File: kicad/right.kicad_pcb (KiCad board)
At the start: 4 copper layers, 127.3 x 89.6 mm, 159 parts, among them M2 MountingHole_2.2mm_M2, Q1 PMF170XP,115, Q2 FS8205A_C2830320, SW1 TS-1088-AR02016, U1 TLV7031QDCKRQ1, U2 E73-2G4M08S1C, U3 SN74LVC1G74DQER, U4 S2B-PH-K-S(LF)(SN), U5 BL8573CS8TR, U6 DW01A_C42380662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

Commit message: started left
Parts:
- moved REF** 0.21 mm to (58.0, 38.2)
- moved USBC1 0.05 mm to (51.5, 30.7)

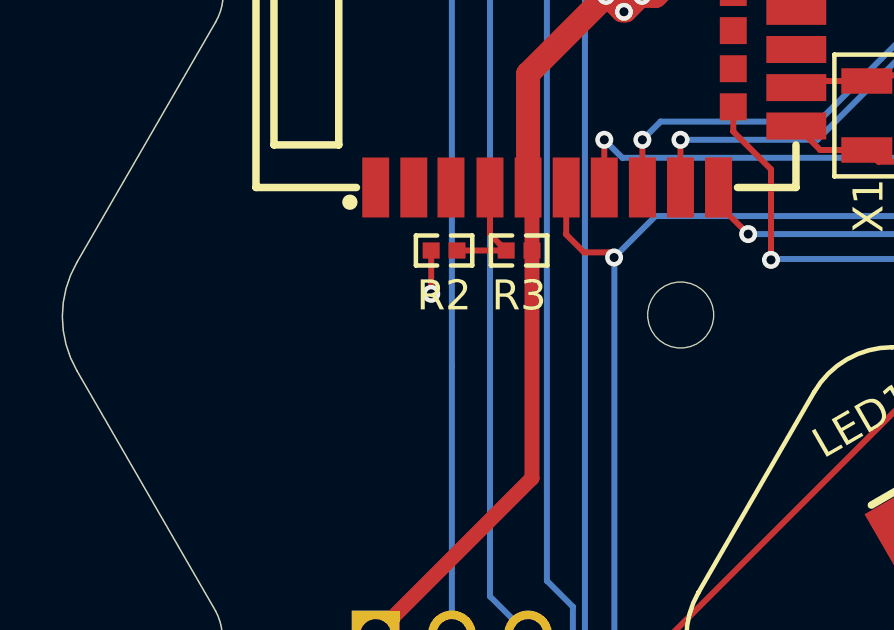
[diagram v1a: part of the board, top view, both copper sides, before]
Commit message: moved  one mounting hole
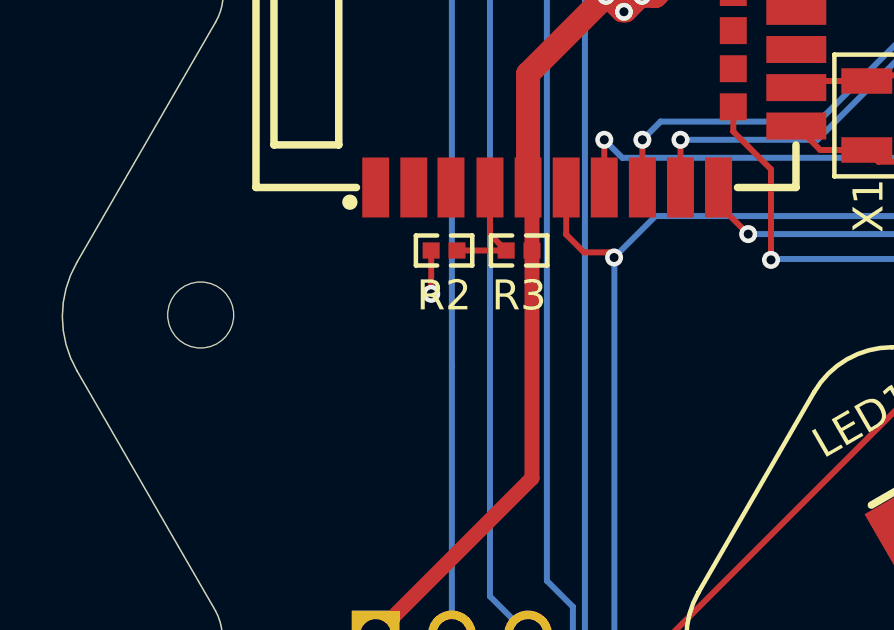
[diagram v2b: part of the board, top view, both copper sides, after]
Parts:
- moved REF** 16.0 mm to (24.7, 91.9)
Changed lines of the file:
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@@
 	(footprint "MountingHole:MountingHole_2.2mm_M2"
 		(layer "F.Cu")
-		(at 40.7 91.9174)
+		(at 24.7 91.9174)
 		(descr "Mounting Hole 2.2mm, M2, no annular, generated by kicad-footprint-generator mountinghole.py")
 		(tags "mountinghole M2")

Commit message: ...
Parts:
- added R17: RC0402FR-071ML, easyeda2kicad:R0402, B.Cu at (43.7, 58.9)
- added R18: WR04W2494FTL, easyeda2kicad:R0402, B.Cu at (41.5, 58.9)
- moved H1 5.00 mm to (33.1, 97.6)
- moved L1 1.08 mm to (46.5, 74.4)
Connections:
- U2 pad 1: /COL7 -> /SWBCLK
- U2 pad 15: unconnected-(U2-AI3-Pad15) -> /LED_EN
- U2 pad 16: unconnected-(U2-P0.08-Pad16) -> /LED_SDA
- U2 pad 17: /COL6 -> /LED_SCL
- U2 pad 2: unconnected-(U2-P1.10-Pad2) -> /SWDIO
- U2 pad 37: /SWDIO -> unconnected-(U2-SWD-Pad37)
- U2 pad 39: /SWBCLK -> unconnected-(U2-SWC-Pad39)
- U2 pad 40: unconnected-(U2-P1.04-Pad40) -> /PWR_BTN_PRESS
- U2 pad 7: /LED_EN -> unconnected-(U2-AI0-Pad7)
- U2 pad 8: /LED_SDA -> unconnected-(U2-AI5-Pad8)
- U2 pad 9: /LED_SCL -> /ROW4
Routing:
- net /ROW4: track 76.2 -> 104.4 mm, vias 0 -> 1
- net /PWR_BTN_PRESS: track 0.00 -> 28.0 mm, vias 0 -> 1
- net /SWBCLK: track 31.3 -> 11.0 mm, vias 1 -> 0
- net /SWDIO: track 31.9 -> 12.3 mm, vias 1 -> 0
- net GND: track 125.1 -> 110.7 mm, vias 47 -> 49
- net /LED_EN: track 20.7 -> 9.42 mm, vias 2 -> 0
- net /LED_SCL: track 17.0 -> 9.77 mm, vias 2 -> 0
- net /LED_SDA: track 19.9 -> 15.3 mm
- net /PWR_BTN: track 32.6 -> 35.0 mm
- net /COL5: track 118.9 -> 119.8 mm
- net Net-(U2-DCH): track 1.93 -> 2.73 mm
- net /VDD_nRF: track 54.0 -> 53.3 mm
- net /PWR: track 92.5 -> 93.0 mm

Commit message: left wiring done... right changed to shmitt inctead of comparator... need to do same on left... fixing of right in progress
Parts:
- removed the R4 at (56.3, 56.9)
- removed the R5 at (49.3, 58.8)
- removed component_case_outline (x5), component_safe_space (x3): , hexcaps:PG1350_hotswap
- R6: value RC0402FR-071ML -> 0402WGF1604TCE
- U1: value TLV7031QDCKRQ1 -> SN74LVC1G17DBVR; footprint easyeda2kicad:SC-70-5_L2.0-W1.3-P0.65-LS2.1-BR -> easyeda2kicad:SOT-23-5_L3.0-W1.7-P0.95-LS2.8-BR
- moved R6 6.85 mm to (56.2, 56.9), turned to -90 degrees
- moved U1 1.12 mm to (51.6, 58.9), turned to 180 degrees
- renumbered R17 to R1, R18 to R2, R1 to R3, R2 to R4, R3 to R5
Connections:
- C2 pad 1: Net-(U1-IN+) -> Net-(U1-A)
- D1 pad 2: Net-(U1-IN+) -> Net-(U1-A)
- R6 pad 2: Net-(U1-IN-) -> Net-(U1-A)
- U1 pad 1: Net-(U1-OUT) -> unconnected-(U1-N.C-Pad1)
- U1 pad 2: GND -> Net-(U1-A)
- U1 pad 3: Net-(U1-IN+) -> GND
- U1 pad 4: Net-(U1-IN-) -> Net-(U1-Y)
- U3 pad 1: Net-(U1-OUT) -> Net-(U1-Y)
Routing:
- net Net-(U1-A): track 0.00 -> 7.23 mm
- net Net-(U1-IN+): track 4.11 -> 0.00 mm
- net Net-(U1-IN-): track 2.86 -> 0.00 mm
- net Net-(U1-Y): track 0.00 -> 2.81 mm
- net Net-(U1-OUT): track 2.37 -> 0.00 mm
- net GND: track 110.7 -> 112.6 mm
- net /PWR_BTN: track 35.0 -> 33.8 mm

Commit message: pcb done. schematick done. need to double check schematick and ask in discord about pcb... but else done
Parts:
- removed M2: MountingHole_2.2mm_M2, MountingHole:MountingHole_2.2mm_M2
- removed R3: RC0402FR-07100KL, easyeda2kicad:R0402
- removed the REF** at (58.0, 38.2)
- removed the REF** at (24.7, 91.9)
- added R1: RC0402FR-07100KL, easyeda2kicad:R0402, B.Cu at (48.8, 56.8)
- added REF**: MountingHole_2.2mm_M2_Pad, MountingHole:MountingHole_2.2mm_M2_Pad, F.Cu at (132.3, 70.4)
- added REF**: MountingHole_2.2mm_M2_Pad, MountingHole:MountingHole_2.2mm_M2_Pad, F.Cu at (76.4, 102.7)
- added REF**: MountingHole_2.2mm_M2_Pad, MountingHole:MountingHole_2.2mm_M2_Pad, F.Cu at (95.0, 48.9)
- R6: value 0402WGF1604TCE -> WR04W2494FTL
- moved R6 7.91 mm to (48.4, 58.4)
- moved D1 2.82 mm to (54.4, 59.8), turned to 90 degrees
- moved C2 1.08 mm to (54.4, 58.0), turned to 90 degrees
- moved U1 0.49 mm to (51.1, 58.9)
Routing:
- net /PWR_BTN: track 33.8 -> 24.1 mm
- net GND: track 112.6 -> 106.7 mm
- net /COL5: track 119.8 -> 122.8 mm
- net /ROW3: track 156.1 -> 153.8 mm
- net /ROW4: track 104.4 -> 102.7 mm
- net /LED2: track 98.9 -> 100.3 mm
- net /LED7: track 41.9 -> 40.5 mm
- net /LED8: track 84.6 -> 83.3 mm
- net Net-(F1-Pad1): vias 8 -> 6
